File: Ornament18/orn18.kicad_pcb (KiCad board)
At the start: 2 copper layers, 50 x 50 mm, 13 parts, among them SW1 SW_Push, U1 ATTINY13A-SSU, U2 74LS138

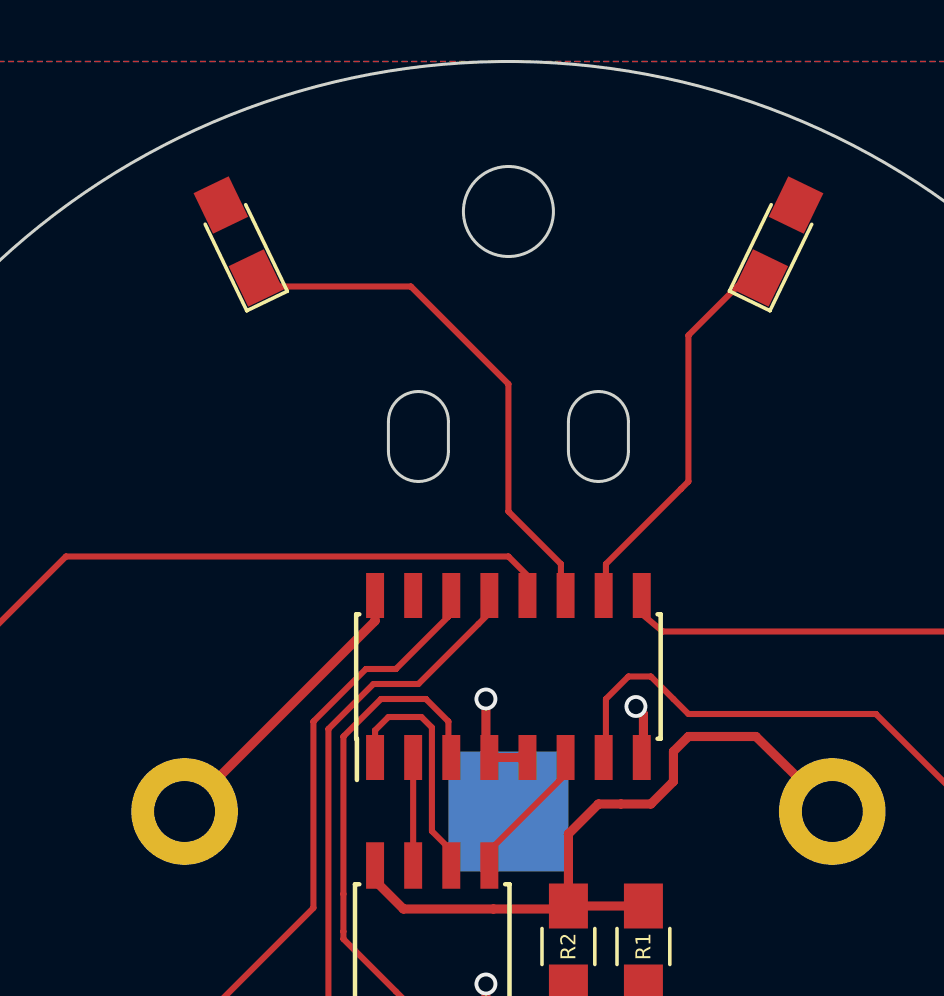
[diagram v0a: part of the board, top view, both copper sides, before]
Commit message: add mechanical holes; add .gitignore
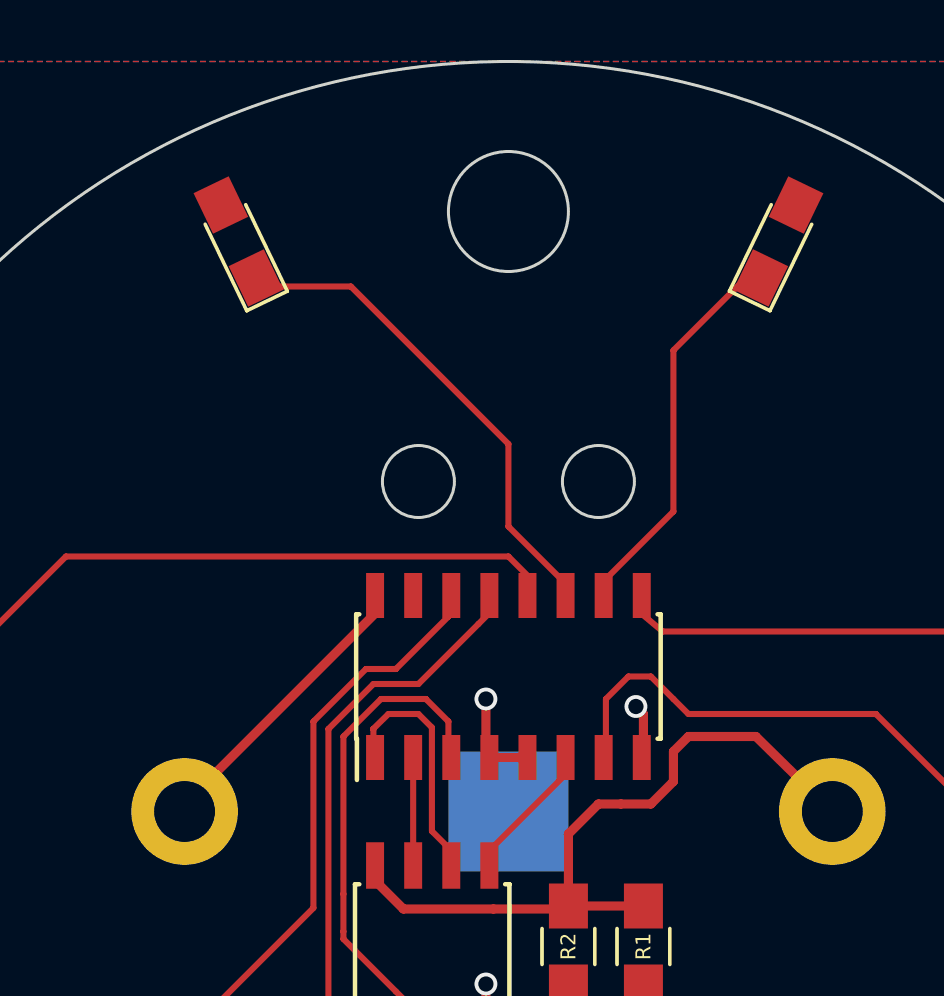
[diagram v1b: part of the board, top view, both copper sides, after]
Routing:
- net Net-(D4-Pad1): track 17.9 -> 16.7 mm
- net Net-(D5-Pad1): track 12.7 -> 13.3 mm
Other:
- outline, holes or cut-outs redrawn
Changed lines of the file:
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@@
     (area 114.949999 74.949999 165.050001 125.050001)
     (thickness 1.6)
-    (drawings 14)
-    (tracks 131)
+    (drawings 4)
+    (tracks 130)
     (zones 0)
     (modules 13)
@@
     (pad_to_mask_clearance 0)
     (aux_axis_origin 0 0)
-    (visible_elements FFFFFF7F)
+    (visible_elements FFFFF77F)
     (pcbplotparams
       (layerselection 0x00030_80000001)
@@
     )
   )
-  (gr_line (start 144 87) (end 144 88) (angle 90) (layer Edge.Cuts) (width 0.1))
-  (gr_line (start 142 87) (end 142 88) (angle 90) (layer Edge.Cuts) (width 0.1))
-  (gr_arc (start 143 87) (end 143 86) (angle 90) (layer Edge.Cuts) (width 0.1))
-  (gr_arc (start 143 87) (end 142 87) (angle 90) (layer Edge.Cuts) (width 0.1))
-  (gr_arc (start 143 88) (end 144 88) (angle 90) (layer Edge.Cuts) (width 0.1))
-  (gr_arc (start 143 88) (end 143 89) (angle 90) (layer Edge.Cuts) (width 0.1))
-  (gr_line (start 138 88) (end 138 87) (angle 90) (layer Edge.Cuts) (width 0.1))
-  (gr_line (start 136 87) (end 136 88) (angle 90) (layer Edge.Cuts) (width 0.1))
-  (gr_arc (start 137 87) (end 137 86) (angle 90) (layer Edge.Cuts) (width 0.1))
-  (gr_arc (start 137 87) (end 136 87) (angle 90) (layer Edge.Cuts) (width 0.1))
-  (gr_arc (start 137 88) (end 138 88) (angle 90) (layer Edge.Cuts) (width 0.1))
-  (gr_arc (start 137 88) (end 137 89) (angle 90) (layer Edge.Cuts) (width 0.1))
-  (gr_circle (center 140 80) (end 140 81.5) (layer Edge.Cuts) (width 0.1))
+  (gr_circle (center 137 89) (end 137 90.2) (layer Edge.Cuts) (width 0.1))
+  (gr_circle (center 143 89) (end 143 90.2) (layer Edge.Cuts) (width 0.1))
+  (gr_circle (center 140 80) (end 140 82) (layer Edge.Cuts) (width 0.1))
   (gr_circle (center 140 100) (end 140 125) (layer Edge.Cuts) (width 0.1))
   (segment (start 144.445 98.2) (end 144.5 98.145) (width 0.3048) (layer F.Cu) (net 1))
@@
   (segment (start 136.5 103.25) (end 139.5 103.25) (width 0.3048) (layer F.Cu) (net 2))
   (segment (start 135.5 102.25) (end 136.5 103.25) (width 0.3048) (layer F.Cu) (net 2))
-  (segment (start 129.205 100) (end 135.555 93.65) (width 0.3048) (layer F.Cu) (net 2))
-  (segment (start 135.555 93.65) (end 135.555 92.8) (width 0.3048) (layer F.Cu) (net 2))
+  (segment (start 129.205 99.75) (end 135.555 93.4) (width 0.3048) (layer F.Cu) (net 2))
+  (segment (start 135.555 93.4) (end 135.555 92.8) (width 0.3048) (layer F.Cu) (net 2))
   (segment (start 142 103.15) (end 144.5 103.15) (width 0.3048) (layer F.Cu) (net 2))
   (segment (start 150.795 100) (end 148.25 97.5) (width 0.3048) (layer F.Cu) (net 2))
@@
   (segment (start 140 91.5) (end 125.25 91.5) (width 0.2032) (layer F.Cu) (net 6))
   (segment (start 125.25 91.5) (end 121.25 95.5) (width 0.2032) (layer F.Cu) (net 6))
-  (segment (start 131.58544 82.216454) (end 131.868986 82.5) (width 0.2032) (layer F.Cu) (net 7) (status 400000))
-  (segment (start 141.75 91.75) (end 141.75 92.645) (width 0.2032) (layer F.Cu) (net 7))
-  (segment (start 140 90) (end 141.75 91.75) (width 0.2032) (layer F.Cu) (net 7))
-  (segment (start 140 85.75) (end 140 90) (width 0.2032) (layer F.Cu) (net 7))
-  (segment (start 136.75 82.5) (end 140 85.75) (width 0.2032) (layer F.Cu) (net 7))
-  (segment (start 131.868986 82.5) (end 136.75 82.5) (width 0.2032) (layer F.Cu) (net 7))
+  (segment (start 131.58544 82.216454) (end 131.868986 82.5) (width 0.2032) (layer F.Cu) (net 7))
+  (segment (start 141.75 92.25) (end 141.75 92.645) (width 0.2032) (layer F.Cu) (net 7))
+  (segment (start 140 90.5) (end 141.75 92.25) (width 0.2032) (layer F.Cu) (net 7))
+  (segment (start 140 87.75) (end 140 90.5) (width 0.2032) (layer F.Cu) (net 7))
+  (segment (start 134.75 82.5) (end 140 87.75) (width 0.2032) (layer F.Cu) (net 7))
+  (segment (start 131.868986 82.5) (end 134.75 82.5) (width 0.2032) (layer F.Cu) (net 7))
   (segment (start 141.75 92.645) (end 141.905 92.8) (width 0.2032) (layer F.Cu) (net 7))
   (segment (start 141.905 92.8) (end 142 92.705) (width 0.2032) (layer F.Cu) (net 7))
-  (segment (start 143.25 91.75) (end 143.25 91.75) (width 0.2032) (layer F.Cu) (net 8))
-  (segment (start 148.412438 81.71543) (end 146 84.127868) (width 0.2032) (layer F.Cu) (net 8))
-  (segment (start 145.75 89.25) (end 143.25 91.75) (width 0.2032) (layer F.Cu) (net 8))
-  (segment (start 146 89) (end 145.75 89.25) (width 0.2032) (layer F.Cu) (net 8))
-  (segment (start 146 84.127868) (end 146 89) (width 0.2032) (layer F.Cu) (net 8))
-  (segment (start 143.25 91.75) (end 143.25 92.25) (width 0.2032) (layer F.Cu) (net 8))
+  (segment (start 143.175 92.8) (end 143.25 92.725) (width 0.2032) (layer F.Cu) (net 8))
+  (segment (start 143.25 92.725) (end 143.25 92.25) (width 0.2032) (layer F.Cu) (net 8))
+  (segment (start 143.25 92.25) (end 145.5 90) (width 0.2032) (layer F.Cu) (net 8))
+  (segment (start 145.5 90) (end 145.5 84.627868) (width 0.2032) (layer F.Cu) (net 8))
+  (segment (start 145.5 84.627868) (end 148.412438 81.71543) (width 0.2032) (layer F.Cu) (net 8))
   (segment (start 144.25 93.25) (end 145.145 94) (width 0.2032) (layer F.Cu) (net 9))
   (segment (start 157.134458 94) (end 158.683548 95.54909) (width 0.2032) (layer F.Cu) (net 9))
@@
   (segment (start 152.25 96.75) (end 155.25 99.75) (width 0.2032) (layer F.Cu) (net 10))
   (segment (start 155.25 99.75) (end 155.25 111.962816) (width 0.2032) (layer F.Cu) (net 10))
-  (segment (start 155.25 111.962816) (end 155.444947 112.157763) (width 0.2032) (layer F.Cu) (net 10) (status 800000))
+  (segment (start 155.25 111.962816) (end 155.444947 112.157763) (width 0.2032) (layer F.Cu) (net 10))
   (segment (start 142.25 111.25) (end 142.75 111.75) (width 0.2032) (layer F.Cu) (net 11))
   (segment (start 142.75 111.75) (end 143.25 111.75) (width 0.2032) (layer F.Cu) (net 11))
@@
   (segment (start 139.365 101.3) (end 141.905 98.76) (width 0.2032) (layer F.Cu) (net 14))
   (segment (start 141.905 98.76) (end 141.905 98.2) (width 0.2032) (layer F.Cu) (net 14) (status 20))
-  (segment (start 135.55 97.3) (end 135.555 97.305) (width 0.2032) (layer F.Cu) (net 15))
+  (segment (start 135.495 97.245) (end 135.5 97.25) (width 0.2032) (layer F.Cu) (net 15))
   (segment (start 137.45 100.655) (end 137.45 97.2) (width 0.2032) (layer F.Cu) (net 15))
-  (segment (start 137.45 97.2) (end 137.1 96.85) (width 0.2032) (layer F.Cu) (net 15))
-  (segment (start 137.1 96.85) (end 136.15 96.85) (width 0.2032) (layer F.Cu) (net 15))
-  (segment (start 136.15 96.85) (end 136 96.85) (width 0.2032) (layer F.Cu) (net 15))
-  (segment (start 136 96.85) (end 135.55 97.3) (width 0.2032) (layer F.Cu) (net 15))
+  (segment (start 137.45 97.2) (end 137 96.75) (width 0.2032) (layer F.Cu) (net 15))
+  (segment (start 137 96.75) (end 136.25 96.75) (width 0.2032) (layer F.Cu) (net 15))
+  (segment (start 136.25 96.75) (end 136 96.75) (width 0.2032) (layer F.Cu) (net 15))
+  (segment (start 136 96.75) (end 135.495 97.245) (width 0.2032) (layer F.Cu) (net 15))
   (segment (start 138.095 101.3) (end 137.45 100.655) (width 0.2032) (layer F.Cu) (net 15))
-  (segment (start 135.555 97.305) (end 135.555 98.2) (width 0.2032) (layer F.Cu) (net 15))
+  (segment (start 135.5 97.25) (end 135.5 98) (width 0.2032) (layer F.Cu) (net 15))
   (segment (start 138.095 101.3) (end 138.1 101.295) (width 0.2032) (layer F.Cu) (net 15))
   (segment (start 136.825 101.8) (end 136.825 98.2) (width 0.2032) (layer F.Cu) (net 16) (status 20))
